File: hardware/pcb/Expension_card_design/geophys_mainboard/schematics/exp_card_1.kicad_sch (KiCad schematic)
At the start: 7 parts, among them J1 550910274

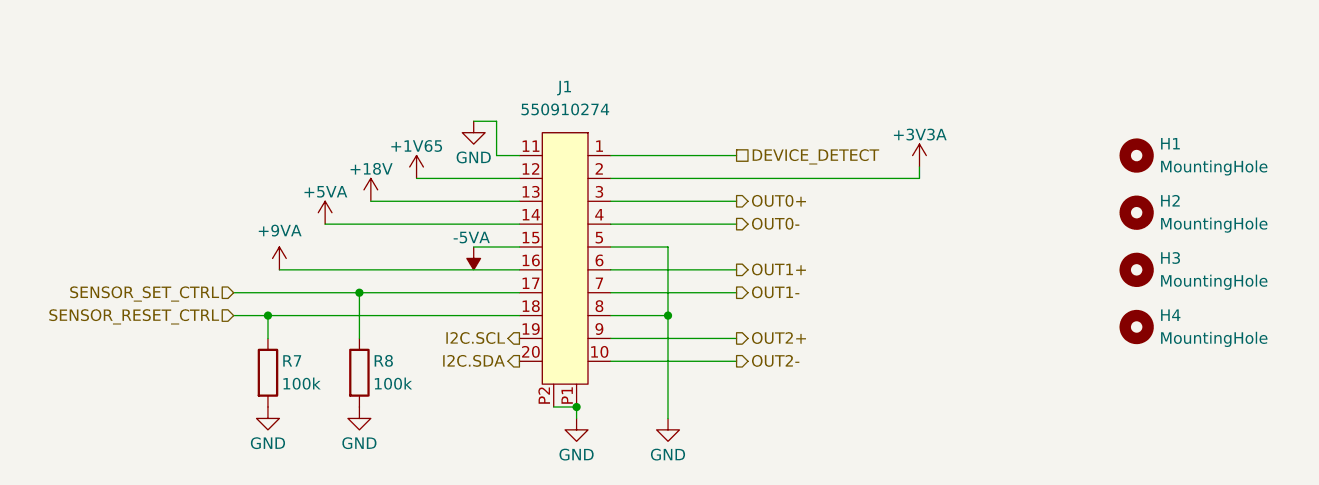
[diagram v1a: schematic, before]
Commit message: Backup avant deletion offset/dac
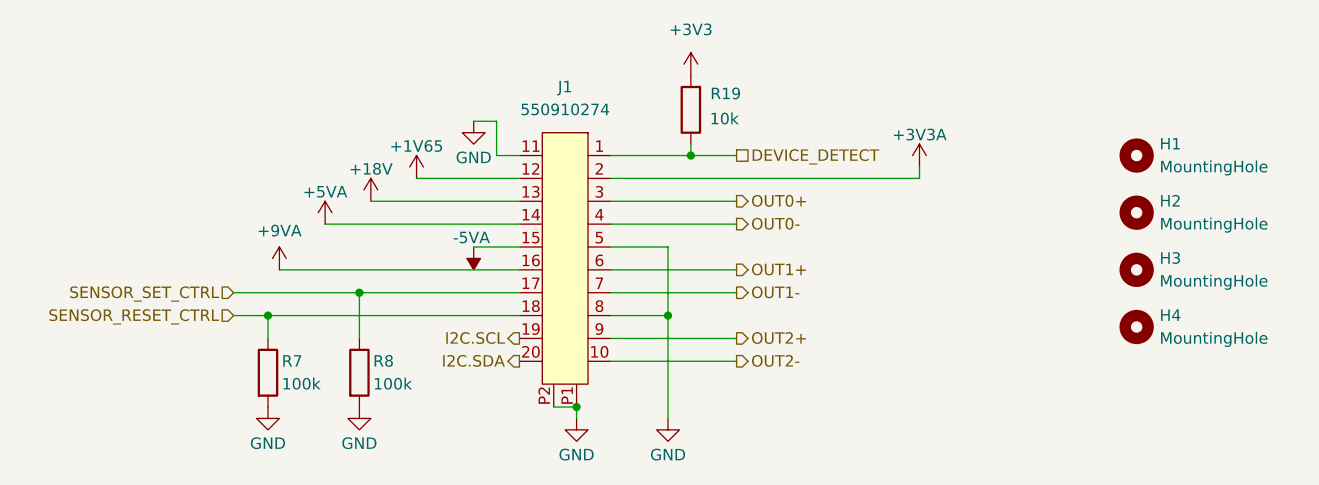
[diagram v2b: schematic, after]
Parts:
- added R19: 10k, Resistor_SMD:R_0603_1608Metric, symbol Device:R
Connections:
- net DEVICE_DETECT: now also R19.1
- new net +3V3: R19.2

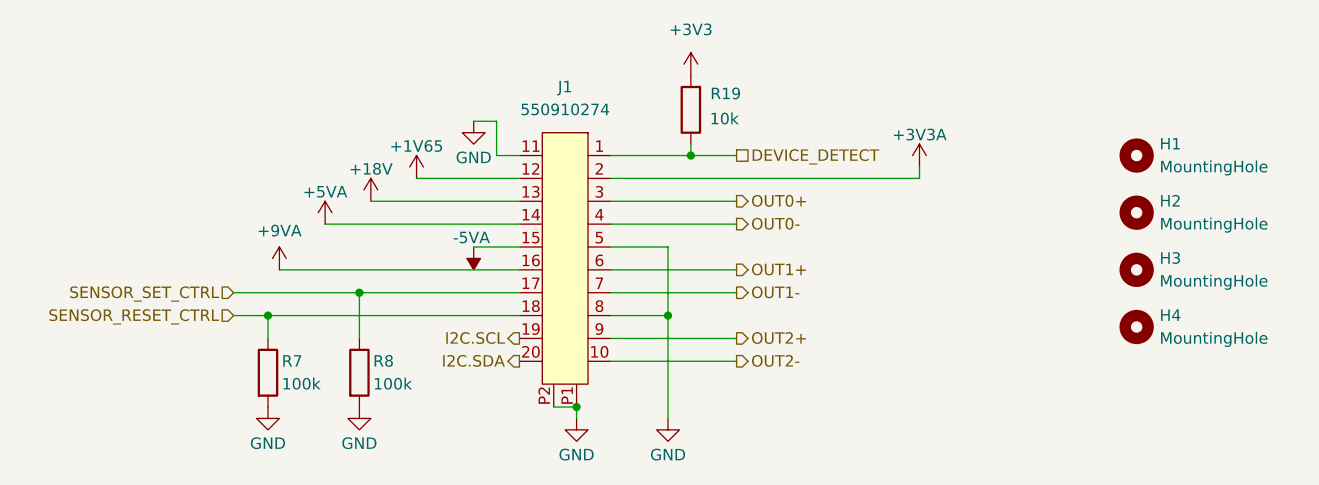
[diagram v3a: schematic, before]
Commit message: calibration on the z and x axis
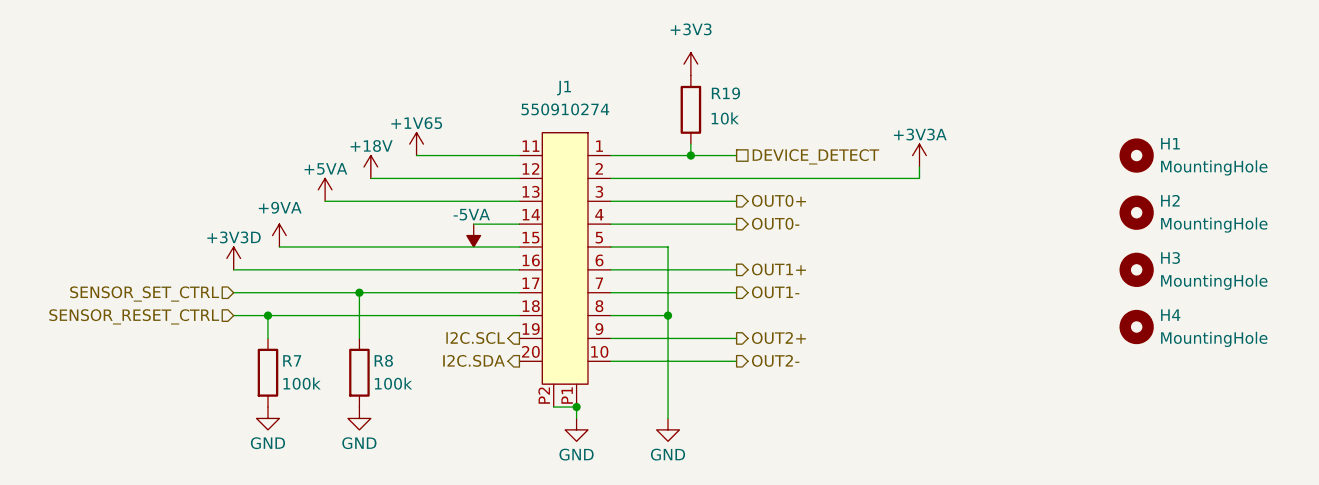
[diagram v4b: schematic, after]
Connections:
- net +18V: now also J1.12; no longer J1.13
- net +1V65: now also J1.11; no longer J1.12
- net +5VA: now also J1.13; no longer J1.14
- net +9VA: now also J1.15; no longer J1.16
- net -5VA: now also J1.14; no longer J1.15
- net GND: no longer J1.11
- new net +3V3D: J1.16
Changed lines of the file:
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@@
-	(wire
-		(pts
-			(xy 128.27 87.63) (xy 130.81 87.63)
-		)
-		(stroke
-			(width 0)
-			(type default)
-		)
-	)
 	(wire
 		(pts
@@
 	(wire
 		(pts
-			(xy 130.81 87.63) (xy 130.81 91.44)
-		)
-		(stroke
-			(width 0)
-			(type default)
-		)
-	)
-	(wire
-		(pts
 			(xy 101.6 106.68) (xy 115.57 106.68)
 		)
@@
 	(wire
 		(pts
-			(xy 116.84 96.52) (xy 133.35 96.52)
+			(xy 116.84 93.98) (xy 133.35 93.98)
 		)
 		(stroke
@@
 	(wire
 		(pts
-			(xy 128.27 101.6) (xy 133.35 101.6)
-		)
-		(stroke
-			(width 0)
-			(type default)
-		)
-	)
-	(wire
-		(pts
-			(xy 106.68 104.14) (xy 133.35 104.14)
+			(xy 128.27 99.06) (xy 133.35 99.06)
+		)
+		(stroke
+			(width 0)
+			(type default)
+		)
+	)
+	(wire
+		(pts
+			(xy 106.68 101.6) (xy 133.35 101.6)
 		)
 		(stroke
@@
 	(wire
 		(pts
-			(xy 121.92 93.98) (xy 133.35 93.98)
-		)
-		(stroke
-			(width 0)
-			(type default)
-		)
-	)
-	(wire
-		(pts
-			(xy 111.76 99.06) (xy 133.35 99.06)
+			(xy 121.92 91.44) (xy 133.35 91.44)
+		)
+		(stroke
+			(width 0)
+			(type default)
+		)
+	)
+	(wire
+		(pts
+			(xy 111.76 96.52) (xy 133.35 96.52)
 		)
 		(stroke
@@
 	(wire
 		(pts
-			(xy 130.81 91.44) (xy 133.35 91.44)
-		)
-		(stroke
-			(width 0)
-			(type default)
-		)
-	)
-	(wire
-		(pts
 			(xy 152.4 91.44) (xy 157.48 91.44)
 		)
@@
 		(pts
 			(xy 101.6 109.22) (xy 105.41 109.22)
+		)
+		(stroke
+			(width 0)
+			(type default)
+		)
+	)
+	(wire
+		(pts
+			(xy 101.6 104.14) (xy 133.35 104.14)
 		)
 		(stroke
@@
 	(symbol
 		(lib_id "power:GND")
-		(at 128.27 87.63 0)
-		(unit 1)
-		(exclude_from_sim no)
-		(in_bom yes)
-		(on_board yes)
-		(dnp no)
-		(property "Reference" "#PWR09"
-			(at 128.27 93.98 0)
-			(effects
-				(font
-					(size 1.27 1.27)
-				)
-				(hide yes)
-			)
-		)
-		(property "Value" "GND"
-			(at 128.27 91.694 0)
-			(effects
-				(font
-					(size 1.27 1.27)
-				)
-			)
-		)
-		(property "Footprint" ""
-			(at 128.27 87.63 0)
-			(effects
-				(font
-					(size 1.27 1.27)
-				)
-				(hide yes)
-			)
-		)
-		(property "Datasheet" ""
-			(at 128.27 87.63 0)
-			(effects
-				(font
-					(size 1.27 1.27)
-				)
-				(hide yes)
-			)
-		)
-		(property "Description" "Power symbol creates a global label with name \"GND\" , ground"
-			(at 128.27 87.63 0)
-			(effects
-				(font
-					(size 1.27 1.27)
-				)
-				(hide yes)
-			)
-		)
-		(pin "1"
-		)
-		(instances
-			(project "geophys_mainboard"
-				(path "/b5f9ef85-43f0-43d8-a1fd-ed489b1654c1/772043ad-5698-4eec-9f80-f66e77d9ab7d"
-					(reference "#PWR095")
-					(unit 1)
-				)
-				(path "/b5f9ef85-43f0-43d8-a1fd-ed489b1654c1/e4ef580d-161a-4ed6-a9fa-ba1ec5666081"
-					(reference "#PWR09")
-					(unit 1)
-				)
-			)
-		)
-	)
-	(symbol
-		(lib_id "power:GND")
 		(at 149.86 120.65 0)
 		(unit 1)
@@
 	(symbol
 		(lib_id "power:-6V")
-		(at 128.27 101.6 180)
+		(at 128.27 99.06 180)
 		(unit 1)
 		(exclude_from_sim no)
@@
 		(dnp no)
 		(property "Reference" "#PWR014"
-			(at 128.27 97.79 0)
+			(at 128.27 95.25 0)
 			(effects
 				(font
@@
 		)
 		(property "Value" "-5VA"
-			(at 128.016 100.584 0)
+			(at 128.016 98.044 0)
 			(effects
 				(font
@@
 		)
 		(property "Footprint" ""
-			(at 128.27 101.6 0)
+			(at 128.27 99.06 0)
 			(effects
 				(font
@@
 		)
 		(property "Datasheet" ""
-			(at 128.27 101.6 0)
+			(at 128.27 99.06 0)
 			(effects
 				(font
@@
 		)
 		(property "Description" "Power symbol creates a global label with name \"-6V\""
-			(at 128.27 101.6 0)
+			(at 128.27 99.06 0)
 			(effects
 				(font
@@
 	(symbol
 		(lib_id "power:+1V8")
-		(at 116.84 96.52 0)
+		(at 116.84 93.98 0)
 		(unit 1)
 		(exclude_from_sim no)
@@
 		(dnp no)
 		(property "Reference" "#PWR012"
-			(at 116.84 100.33 0)
+			(at 116.84 97.79 0)
 			(effects
 				(font
@@
 		)
 		(property "Value" "+18V"
-			(at 116.84 92.964 0)
+			(at 116.84 90.424 0)
 			(effects
 				(font
@@
 		)
 		(property "Footprint" ""
-			(at 116.84 96.52 0)
+			(at 116.84 93.98 0)
 			(effects
 				(font
@@
 		)
 		(property "Datasheet" ""
-			(at 116.84 96.52 0)
+			(at 116.84 93.98 0)
 			(effects
 				(font
@@
 		)
 		(property "Description" "Power symbol creates a global label with name \"+1V8\""
-			(at 116.84 96.52 0)
+			(at 116.84 93.98 0)
 			(effects
 				(font
@@
 				(path "/b5f9ef85-43f0-43d8-a1fd-ed489b1654c1/e4ef580d-161a-4ed6-a9fa-ba1ec5666081"
 					(reference "#PWR012")
+					(unit 1)
+				)
+			)
+		)
+	)
+	(symbol
+		(lib_id "power:+3V3")
+		(at 101.6 104.14 0)
+		(unit 1)
+		(exclude_from_sim no)
+		(in_bom yes)
+		(on_board yes)
+		(dnp no)
+		(property "Reference" "#PWR09"
+			(at 101.6 107.95 0)
+			(effects
+				(font
+					(size 1.27 1.27)
+				)
+				(hide yes)
+			)
+		)
+		(property "Value" "+3V3D"
+			(at 101.6 100.584 0)
+			(effects
+				(font
+					(size 1.27 1.27)
+				)
+			)
+		)
+		(property "Footprint" ""
+			(at 101.6 104.14 0)
+			(effects
+				(font
+					(size 1.27 1.27)
+				)
+				(hide yes)
+			)
+		)
+		(property "Datasheet" ""
+			(at 101.6 104.14 0)
+			(effects
+				(font
+					(size 1.27 1.27)
+				)
+				(hide yes)
+			)
+		)
+		(property "Description" "Power symbol creates a global label with name \"+3V3\""
+			(at 101.6 104.14 0)
+			(effects
+				(font
+					(size 1.27 1.27)
+				)
+				(hide yes)
+			)
+		)
+		(pin "1"
+		)
+		(instances
+			(project "geophys_mainboard"
+				(path "/b5f9ef85-43f0-43d8-a1fd-ed489b1654c1/772043ad-5698-4eec-9f80-f66e77d9ab7d"
+					(reference "#PWR095")
+					(unit 1)
+				)
+				(path "/b5f9ef85-43f0-43d8-a1fd-ed489b1654c1/e4ef580d-161a-4ed6-a9fa-ba1ec5666081"
+					(reference "#PWR09")
 					(unit 1)
 				)
@@
 	(symbol
 		(lib_id "power:+1V0")
-		(at 121.92 93.98 0)
+		(at 121.92 91.44 0)
 		(unit 1)
 		(exclude_from_sim no)
@@
 		(dnp no)
 		(property "Reference" "#PWR011"
-			(at 121.92 97.79 0)
+			(at 121.92 95.25 0)
 			(effects
 				(font
@@
 		)
 		(property "Value" "+1V65"
-			(at 121.92 90.424 0)
+			(at 121.92 87.884 0)
 			(effects
 				(font
@@
 		)
 		(property "Footprint" ""
-			(at 121.92 93.98 0)
+			(at 121.92 91.44 0)
 			(effects
 				(font
@@
 		)
 		(property "Datasheet" ""
-			(at 121.92 93.98 0)
+			(at 121.92 91.44 0)
 			(effects
 				(font
@@
 		)
 		(property "Description" "Power symbol creates a global label with name \"+1V0\""
-			(at 121.92 93.98 0)
+			(at 121.92 91.44 0)
 			(effects
 				(font
@@
 	(symbol
 		(lib_id "power:+9VA")
-		(at 106.68 104.14 0)
+		(at 106.68 101.6 0)
 		(unit 1)
 		(exclude_from_sim no)
@@
 		(dnp no)
 		(property "Reference" "#PWR015"
-			(at 106.68 107.315 0)
+			(at 106.68 104.775 0)
 			(effects
 				(font
@@
 		)
 		(property "Value" "+9VA"
-			(at 106.68 99.822 0)
+			(at 106.68 97.282 0)
 			(effects
 				(font
@@
 		)
 		(property "Footprint" ""
-			(at 106.68 104.14 0)
+			(at 106.68 101.6 0)
 			(effects
 				(font
@@
 		)
 		(property "Datasheet" ""
-			(at 106.68 104.14 0)
+			(at 106.68 101.6 0)
 			(effects
 				(font
@@
 		)
 		(property "Description" "Power symbol creates a global label with name \"+9VA\""
-			(at 106.68 104.14 0)
+			(at 106.68 101.6 0)
 			(effects
 				(font
@@
 	(symbol
 		(lib_id "power:+10V")
-		(at 111.76 99.06 0)
+		(at 111.76 96.52 0)
 		(unit 1)
 		(exclude_from_sim no)
@@
 		(dnp no)
 		(property "Reference" "#PWR013"
-			(at 111.76 102.87 0)
+			(at 111.76 100.33 0)
 			(effects
 				(font
@@
 		)
 		(property "Value" "+5VA"
-			(at 111.76 95.504 0)
+			(at 111.76 92.964 0)
 			(effects
 				(font
@@
 		)
 		(property "Footprint" ""
-			(at 111.76 99.06 0)
+			(at 111.76 96.52 0)
 			(effects
 				(font
@@
 		)
 		(property "Datasheet" ""
-			(at 111.76 99.06 0)
+			(at 111.76 96.52 0)
 			(effects
 				(font
@@
 		)
 		(property "Description" "Power symbol creates a global label with name \"+10V\""
-			(at 111.76 99.06 0)
-			(effects
-				(font
+			(at 111.76 96.52 0)
+			(effects
+				(font
